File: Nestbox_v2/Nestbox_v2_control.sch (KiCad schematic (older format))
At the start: 23 parts, among them P1 RX/TX, P2 TST/RST, SW1 SMD-BUTTON_2P-3.0X2.5X1.2+0.4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, U1 MSP430FR5969, Y1 Crystal

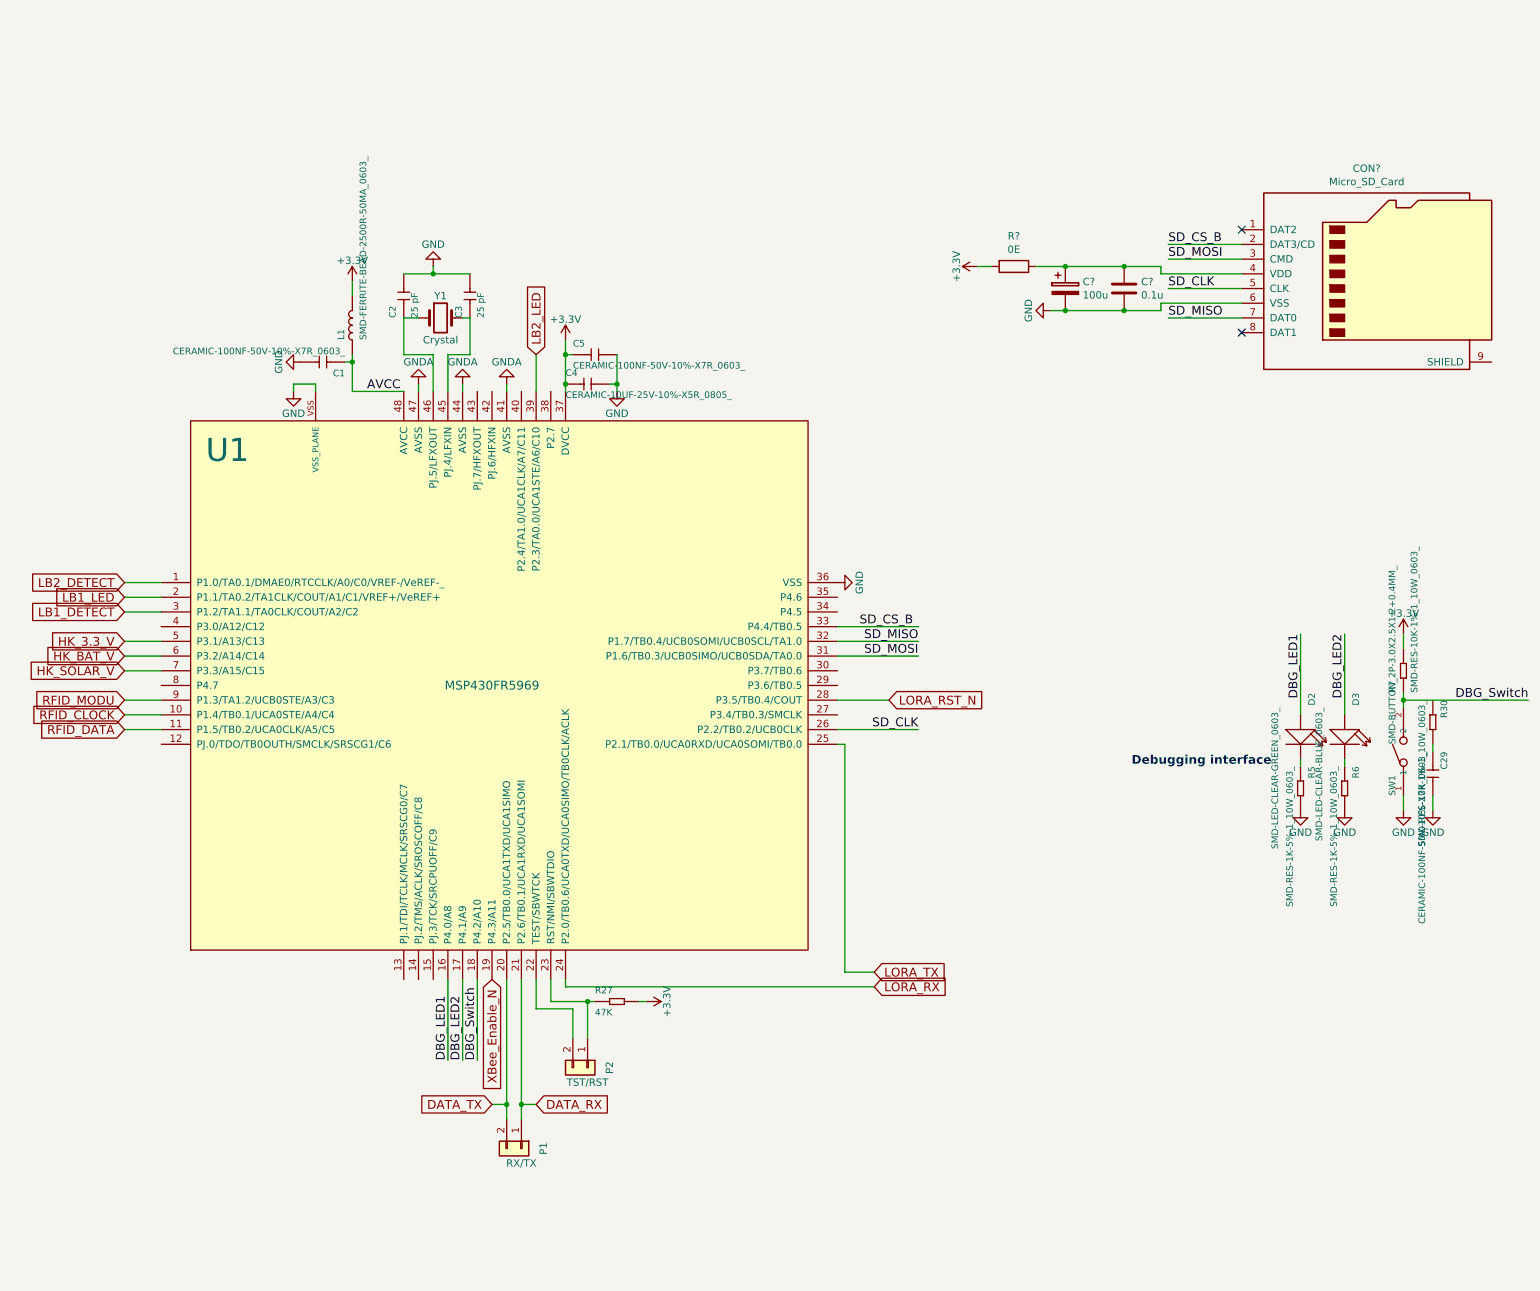
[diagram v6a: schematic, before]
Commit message: Replaces R and C in control schematic with std comp
The R and C components used in the controll schematic where replaced with standard components
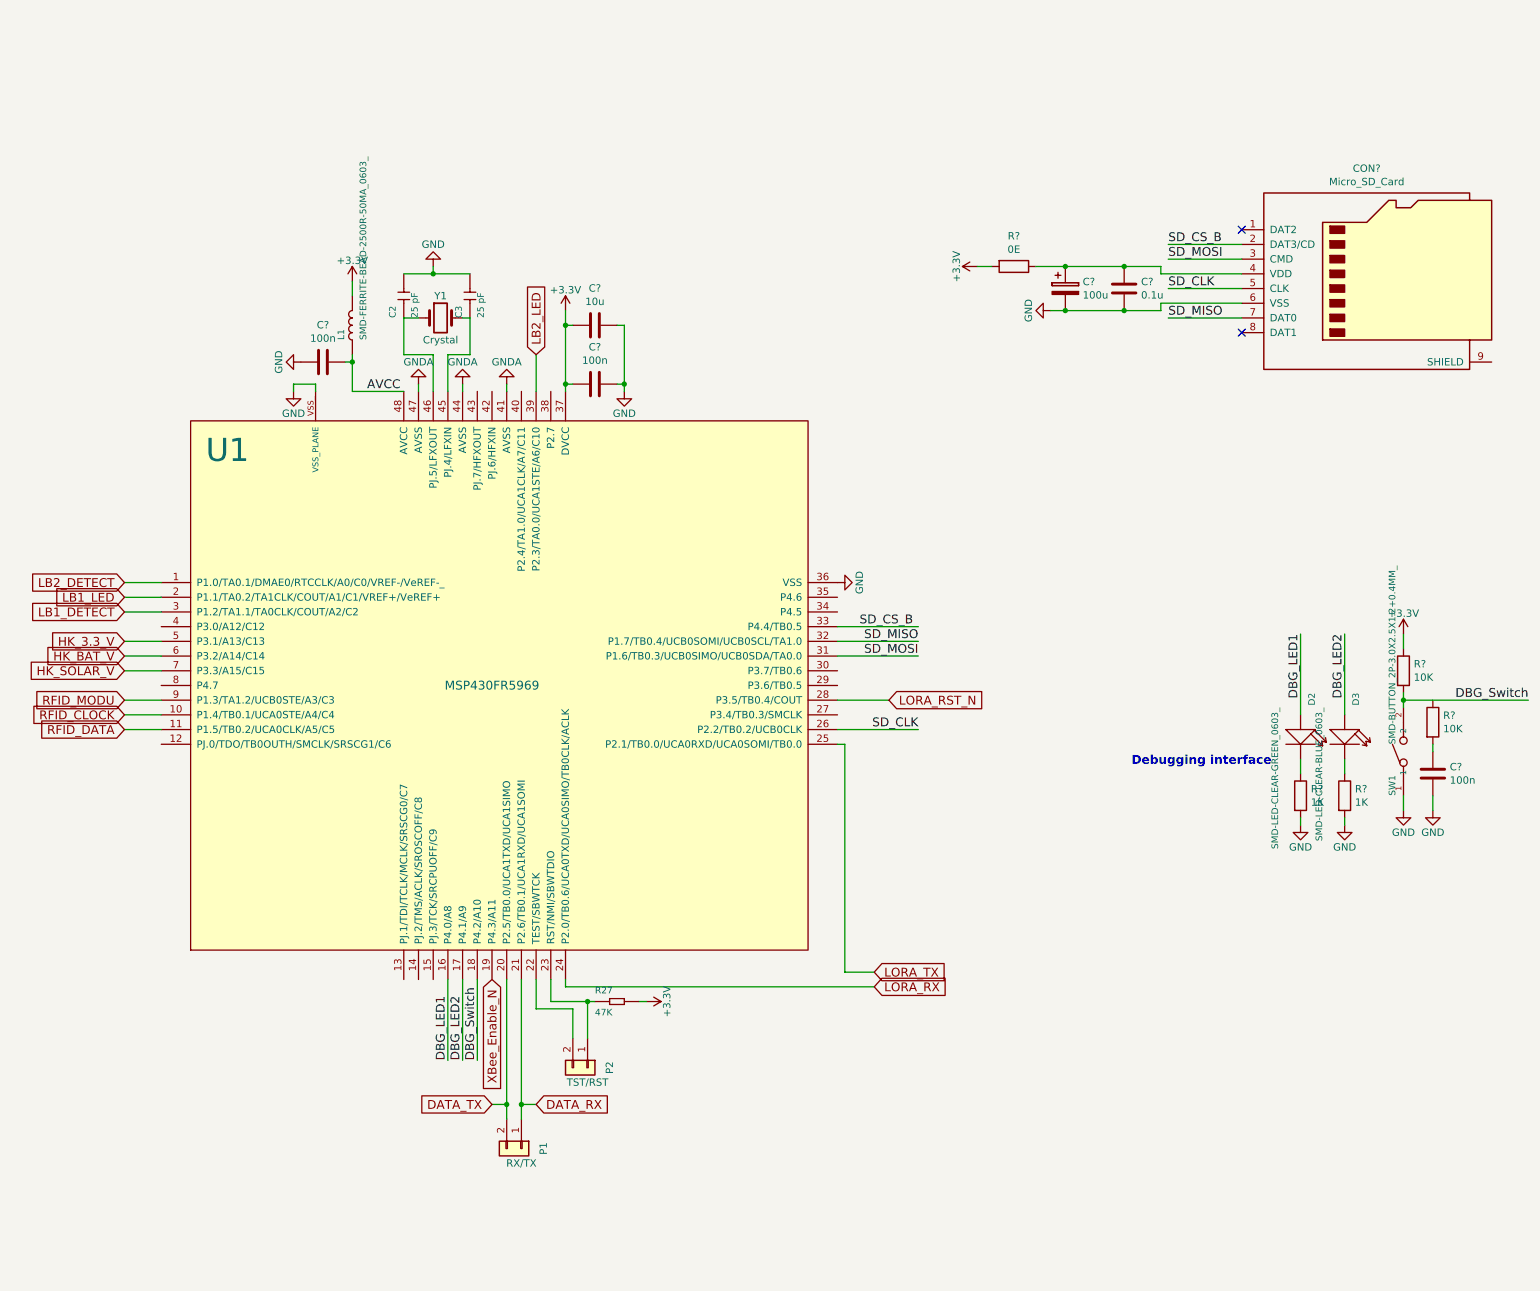
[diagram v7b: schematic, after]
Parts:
- removed C1, C29, C5: CERAMIC-100NF-50V-10%-X7R_0603_, SeeedOPL-Capacitor-2016:C0603, symbol CERAMIC-100NF-50V-10%-X7R_0603_
- removed C4: CERAMIC-10UF-25V-10%-X5R_0805_, SeeedOPL-Capacitor-2016:C0805, symbol CERAMIC-10UF-25V-10%-X5R_0805_
- removed R30, R7: SMD-RES-10K-1%-1_10W_0603_, SeeedOPL-Resistor-2016:R0603, symbol SMD-RES-10K-1%-1_10W_0603_
- removed R5, R6: SMD-RES-1K-5%-1_10W_0603_, SeeedOPL-Resistor-2016:R0603, symbol SMD-RES-1K-5%-1_10W_0603_
- added C? (x3): 100n, symbol C
- added C?: 10u, symbol C
- added R? (x2): 1K, symbol R
- added R? (x2): 10K, symbol R
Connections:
- net +3V3: now also C?.2, C?.2, R?.1
- net AVCC: now also C?.1
- net DBG_Switch: now also R?.2
- net GND: now also C?.1, C?.1, C?.2, C?.2, R?.2, R?.2
- net at D2.-: now also R?.1
- net at D3.-: now also R?.1
- new net: C?.1, R?.2
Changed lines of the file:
@@
 L +3.3V #PWR02
 U 1 1 586418DC
-P 4300 2100
-F 0 "#PWR02" H 4300 1950 50  0001 C CNN
-F 1 "+3.3V" H 4300 2240 50  0000 C CNN
-F 2 "" H 4300 2100 50  0000 C CNN
-F 3 "" H 4300 2100 50  0000 C CNN
-	1    4300 2100
+P 4300 1900
+F 0 "#PWR02" H 4300 1750 50  0001 C CNN
+F 1 "+3.3V" H 4300 2040 50  0000 C CNN
+F 2 "" H 4300 1900 50  0000 C CNN
+F 3 "" H 4300 1900 50  0000 C CNN
+	1    4300 1900
 	1    0    0    -1
 $EndComp
@@
 L GND #PWR05
 U 1 1 58652F3A
-P 4650 2450
-F 0 "#PWR05" H 4650 2200 50  0001 C CNN
-F 1 "GND" H 4650 2300 50  0000 C CNN
-F 2 "" H 4650 2450 50  0000 C CNN
-F 3 "" H 4650 2450 50  0000 C CNN
-	1    4650 2450
+P 4700 2450
+F 0 "#PWR05" H 4700 2200 50  0001 C CNN
+F 1 "GND" H 4700 2300 50  0000 C CNN
+F 2 "" H 4700 2450 50  0000 C CNN
+F 3 "" H 4700 2450 50  0000 C CNN
+	1    4700 2450
 	1    0    0    -1
 $EndComp
@@
 $EndComp
 $Comp
-L SMD-RES-1K-5%-1_10W_0603_ R5
-U 1 1 587B9294
-P 9300 5150
-F 0 "R5" H 9150 5200 45  0000 L BNN
-F 1 "SMD-RES-1K-5%-1_10W_0603_" H 9150 5050 45  0000 L BNN
-F 2 "SeeedOPL-Resistor-2016:R0603" H 9300 5150 40  0001 C CNN
-F 3 "" H 9300 5150 40  0001 C CNN
-F 4 "RC0603JR-071KL" H 9330 5300 20  0001 C CNN "MPN"
-F 5 "301010291" H 9330 5300 20  0001 C CNN "SKU"
-F 6 "" H 9330 5300 20  0001 C CNN "Field6"
-	1    9300 5150
-	0    1    1    0
-$EndComp
-$Comp
-L SMD-RES-1K-5%-1_10W_0603_ R6
-U 1 1 587B92F0
-P 9600 5150
-F 0 "R6" H 9450 5200 45  0000 L BNN
-F 1 "SMD-RES-1K-5%-1_10W_0603_" H 9450 5050 45  0000 L BNN
-F 2 "SeeedOPL-Resistor-2016:R0603" H 9600 5150 40  0001 C CNN
-F 3 "" H 9600 5150 40  0001 C CNN
-F 4 "RC0603JR-071KL" H 9630 5300 20  0001 C CNN "MPN"
-F 5 "301010291" H 9630 5300 20  0001 C CNN "SKU"
-F 6 "" H 9630 5300 20  0001 C CNN "Field6"
-	1    9600 5150
-	0    1    1    0
-$EndComp
-$Comp
-L SMD-RES-10K-1%-1_10W_0603_ R7
-U 1 1 587B94DB
-P 10000 4350
-F 0 "R7" H 9850 4400 45  0000 L BNN
-F 1 "SMD-RES-10K-1%-1_10W_0603_" H 9850 4250 45  0000 L BNN
-F 2 "SeeedOPL-Resistor-2016:R0603" H 10000 4350 40  0001 C CNN
-F 3 "" H 10000 4350 40  0001 C CNN
-F 4 "RC0603FR-0710KL" H 10030 4500 20  0001 C CNN "MPN"
-F 5 "301010299" H 10030 4500 20  0001 C CNN "SKU"
-F 6 "" H 10030 4500 20  0001 C CNN "Field6"
-	1    10000 4350
-	0    -1   -1   0
-$EndComp
-$Comp
 L GND #PWR016
 U 1 1 587B96DD
@@
 L GND #PWR018
 U 1 1 587B97E4
-P 9600 5300
-F 0 "#PWR018" H 9600 5050 50  0001 C CNN
-F 1 "GND" H 9600 5150 50  0000 C CNN
-F 2 "" H 9600 5300 50  0000 C CNN
-F 3 "" H 9600 5300 50  0000 C CNN
-	1    9600 5300
+P 9600 5400
+F 0 "#PWR018" H 9600 5150 50  0001 C CNN
+F 1 "GND" H 9600 5250 50  0000 C CNN
+F 2 "" H 9600 5400 50  0000 C CNN
+F 3 "" H 9600 5400 50  0000 C CNN
+	1    9600 5400
 	1    0    0    -1
 $EndComp
@@
 L GND #PWR019
 U 1 1 587B9834
-P 9300 5300
-F 0 "#PWR019" H 9300 5050 50  0001 C CNN
-F 1 "GND" H 9300 5150 50  0000 C CNN
-F 2 "" H 9300 5300 50  0000 C CNN
-F 3 "" H 9300 5300 50  0000 C CNN
-	1    9300 5300
+P 9300 5400
+F 0 "#PWR019" H 9300 5150 50  0001 C CNN
+F 1 "GND" H 9300 5250 50  0000 C CNN
+F 2 "" H 9300 5400 50  0000 C CNN
+F 3 "" H 9300 5400 50  0000 C CNN
+	1    9300 5400
 	1    0    0    -1
 $EndComp
@@
 AVCC
 Wire Wire Line
-	4300 2100 4300 2450
+	4300 1900 4300 2450
 Connection ~ 4300 2400
-Connection ~ 4300 2200
+Connection ~ 4300 2000
 Wire Wire Line
 	3200 2200 3400 2200
@@
 	0    -1   -1   0
 $EndComp
-$Comp
-L CERAMIC-100NF-50V-10%-X7R_0603_ C5
-U 1 1 587CB67A
-P 4500 2200
-F 0 "C5" H 4350 2250 45  0000 L BNN
-F 1 "CERAMIC-100NF-50V-10%-X7R_0603_" H 4350 2100 45  0000 L BNN
-F 2 "SeeedOPL-Capacitor-2016:C0603" H 4500 2200 60  0001 C CNN
-F 3 "" H 4500 2200 60  0001 C CNN
-F 4 "CC0603KRX7R9BB104" H 4530 2350 20  0001 C CNN "MPN"
-F 5 "302010138" H 4530 2350 20  0001 C CNN "SKU"
-F 6 "" H 4530 2350 20  0001 C CNN "Field6"
-	1    4500 2200
-	1    0    0    -1
-$EndComp
-$Comp
-L CERAMIC-100NF-50V-10%-X7R_0603_ C1
-U 1 1 587CBA36
-P 2650 2250
-F 0 "C1" H 2500 2300 45  0000 L BNN
-F 1 "CERAMIC-100NF-50V-10%-X7R_0603_" H 2500 2150 45  0000 L BNN
-F 2 "SeeedOPL-Capacitor-2016:C0603" H 2650 2250 60  0001 C CNN
-F 3 "" H 2650 2250 60  0001 C CNN
-F 4 "CC0603KRX7R9BB104" H 2680 2400 20  0001 C CNN "MPN"
-F 5 "302010138" H 2680 2400 20  0001 C CNN "SKU"
-F 6 "" H 2680 2400 20  0001 C CNN "Field6"
-	1    2650 2250
-	-1   0    0    1
-$EndComp
-Wire Wire Line
-	4300 2200 4350 2200
-Wire Wire Line
-	4650 2200 4650 2450
-Wire Wire Line
-	4600 2400 4650 2400
-Connection ~ 4650 2400
+Wire Wire Line
+	4300 2000 4350 2000
 $Comp
 L SMD-LED-CLEAR-GREEN_0603_ D2
@@
 $EndComp
 Wire Wire Line
-	9600 5000 9600 4950
-Wire Wire Line
-	9300 5000 9300 4950
+	9600 4950 9600 5050
+Wire Wire Line
+	9300 4950 9300 5050
 $Comp
 L GND #PWR030
@@
 Wire Wire Line
 	2450 2400 2450 2450
-$Comp
-L CERAMIC-10UF-25V-10%-X5R_0805_ C4
-U 1 1 58B8E196
-P 4450 2400
-F 0 "C4" H 4300 2450 45  0000 L BNN
-F 1 "CERAMIC-10UF-25V-10%-X5R_0805_" H 4300 2300 45  0000 L BNN
-F 2 "SeeedOPL-Capacitor-2016:C0805" H 4450 2400 60  0001 C CNN
-F 3 "" H 4450 2400 60  0001 C CNN
-F 4 "CC0805KKX5R8BB106" H 4480 2550 20  0001 C CNN "MPN"
-F 5 "302010178" H 4480 2550 20  0001 C CNN "SKU"
-F 6 "" H 4480 2550 20  0001 C CNN "Field6"
-	1    4450 2400
-	1    0    0    -1
-$EndComp
 Text GLabel 6400 6400 2    60   Input ~ 0
 LORA_TX
@@
 Wire Wire Line
 	4850 6600 4800 6600
-$Comp
-L CERAMIC-100NF-50V-10%-X7R_0603_ C29
-U 1 1 58BF15A3
-P 10200 5050
-F 0 "C29" H 10050 5100 45  0000 L BNN
-F 1 "CERAMIC-100NF-50V-10%-X7R_0603_" H 10050 4950 45  0000 L BNN
-F 2 "SeeedOPL-Capacitor-2016:C0603" H 10200 5050 60  0001 C CNN
-F 3 "" H 10200 5050 60  0001 C CNN
-F 4 "CC0603KRX7R9BB104" H 10230 5200 20  0001 C CNN "MPN"
-F 5 "302010138" H 10230 5200 20  0001 C CNN "SKU"
-F 6 "" H 10230 5200 20  0001 C CNN "Field6"
-	1    10200 5050
-	0    1    1    0
-$EndComp
 Wire Wire Line
 	10200 4850 10200 4850
@@
 Text Label 10850 4550 2    60   ~ 0
 DBG_Switch
-$Comp
-L SMD-RES-10K-1%-1_10W_0603_ R30
-U 1 1 58BF0F5A
-P 10200 4700
-F 0 "R30" H 10050 4750 45  0000 L BNN
-F 1 "SMD-RES-10K-1%-1_10W_0603_" H 10050 4600 45  0000 L BNN
-F 2 "SeeedOPL-Resistor-2016:R0603" H 10200 4700 40  0001 C CNN
-F 3 "" H 10200 4700 40  0001 C CNN
-F 4 "RC0603FR-0710KL" H 10230 4850 20  0001 C CNN "MPN"
-F 5 "301010299" H 10230 4850 20  0001 C CNN "SKU"
-F 6 "" H 10230 4850 20  0001 C CNN "Field6"
-	1    10200 4700
-	0    1    1    0
-$EndComp
 Text GLabel 3800 6450 3    60   Input ~ 0
 XBee_Enable_N
@@
 Wire Wire Line
 	7100 1600 7200 1600
+$Comp
+L R R?
+U 1 1 59FF6DD5
+P 9300 5200
+F 0 "R?" H 9370 5246 50  0000 L CNN
+F 1 "1K" H 9370 5155 50  0000 L CNN
+F 2 "" V 9230 5200 50  0000 C CNN
+F 3 "" H 9300 5200 50  0000 C CNN
+	1    9300 5200
+	1    0    0    -1
+$EndComp
+Wire Wire Line
+	9300 5350 9300 5400
+$Comp
+L R R?
+U 1 1 59FF6FBB
+P 9600 5200
+F 0 "R?" H 9670 5246 50  0000 L CNN
+F 1 "1K" H 9670 5155 50  0000 L CNN
+F 2 "" V 9530 5200 50  0000 C CNN
+F 3 "" H 9600 5200 50  0000 C CNN
+	1    9600 5200
+	1    0    0    -1
+$EndComp
+Wire Wire Line
+	9600 5350 9600 5400
+$Comp
+L R R?
+U 1 1 59FF7355
+P 10200 4700
+F 0 "R?" H 10270 4746 50  0000 L CNN
+F 1 "10K" H 10270 4655 50  0000 L CNN
+F 2 "" V 10130 4700 50  0000 C CNN
+F 3 "" H 10200 4700 50  0000 C CNN
+	1    10200 4700
+	1    0    0    -1
+$EndComp
+$Comp
+L R R?
+U 1 1 59FF739D
+P 10000 4350
+F 0 "R?" H 10070 4396 50  0000 L CNN
+F 1 "10K" H 10070 4305 50  0000 L CNN
+F 2 "" V 9930 4350 50  0000 C CNN
+F 3 "" H 10000 4350 50  0000 C CNN
+	1    10000 4350
+	1    0    0    -1
+$EndComp
+$Comp
+L C C?
+U 1 1 59FF75BA
+P 10200 5050
+F 0 "C?" H 10315 5096 50  0000 L CNN
+F 1 "100n" H 10315 5005 50  0000 L CNN
+F 2 "" H 10238 4900 50  0000 C CNN
+F 3 "" H 10200 5050 50  0000 C CNN
+	1    10200 5050
+	1    0    0    -1
+$EndComp
+$Comp
+L C C?
+U 1 1 59FF79ED
+P 4500 2000
+F 0 "C?" V 4248 2000 50  0000 C CNN
+F 1 "10u" V 4339 2000 50  0000 C CNN
+F 2 "" H 4538 1850 50  0000 C CNN
+F 3 "" H 4500 2000 50  0000 C CNN
+	1    4500 2000
+	0    1    1    0
+$EndComp
+$Comp
+L C C?
+U 1 1 59FF7AC3
+P 4500 2400
+F 0 "C?" V 4248 2400 50  0000 C CNN
+F 1 "100n" V 4339 2400 50  0000 C CNN
+F 2 "" H 4538 2250 50  0000 C CNN
+F 3 "" H 4500 2400 50  0000 C CNN
+	1    4500 2400
+	0    1    1    0
+$EndComp
+Wire Wire Line
+	4300 2400 4350 2400
+Wire Wire Line
+	4650 2000 4700 2000
+Wire Wire Line
+	4700 2000 4700 2450
+Wire Wire Line
+	4650 2400 4700 2400
+Connection ~ 4700 2400
+$Comp
+L C C?
+U 1 1 59FF7E1A
+P 2650 2250
+F 0 "C?" V 2398 2250 50  0000 C CNN
+F 1 "100n" V 2489 2250 50  0000 C CNN
+F 2 "" H 2688 2100 50  0000 C CNN
+F 3 "" H 2650 2250 50  0000 C CNN
+	1    2650 2250
+	0    1    1    0
+$EndComp
 $EndSCHEMATC
